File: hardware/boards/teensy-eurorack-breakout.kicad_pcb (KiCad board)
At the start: 2 copper layers, 64.8 x 109.2 mm, 33 parts, among them J1 Conn_01x08, J2 Conn_01x20, J3 Conn_01x20, SW1 Rotary_Encoder_Switch

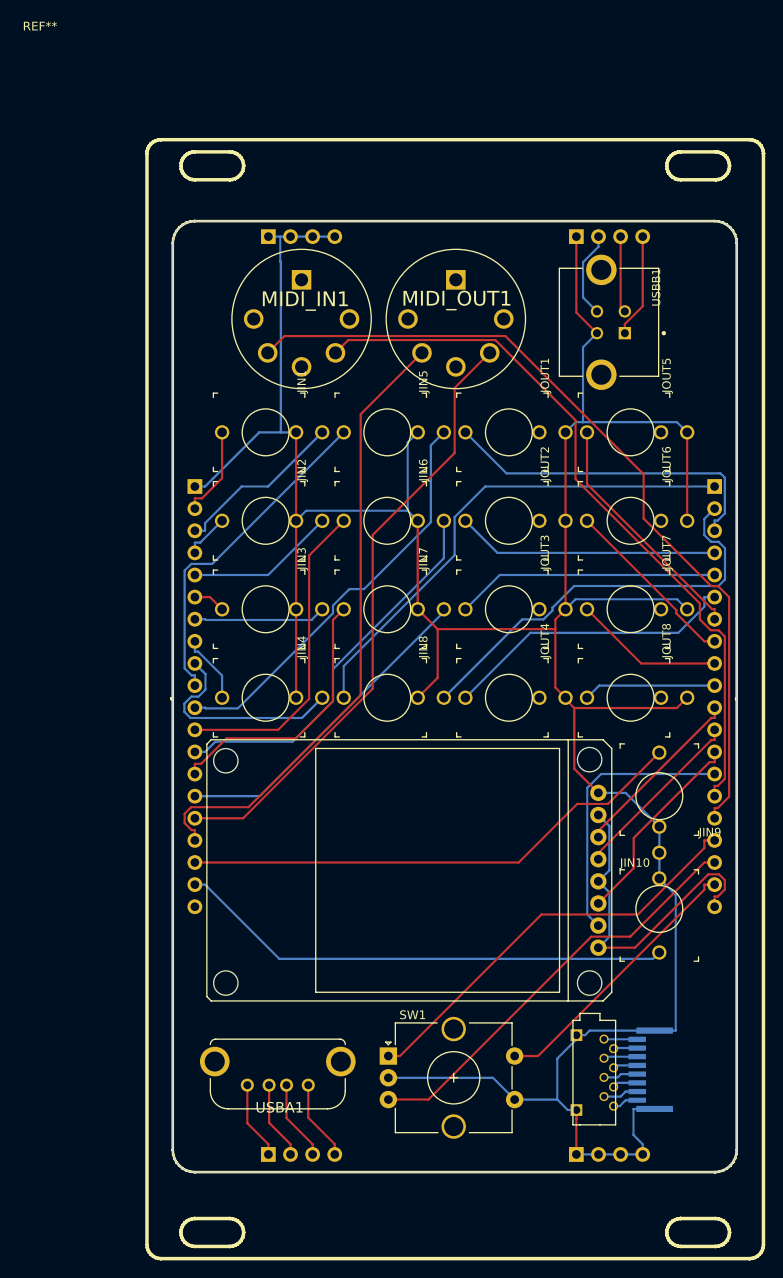
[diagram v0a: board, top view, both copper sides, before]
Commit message: Added jlcpcb parts and changed PCB to 10HP
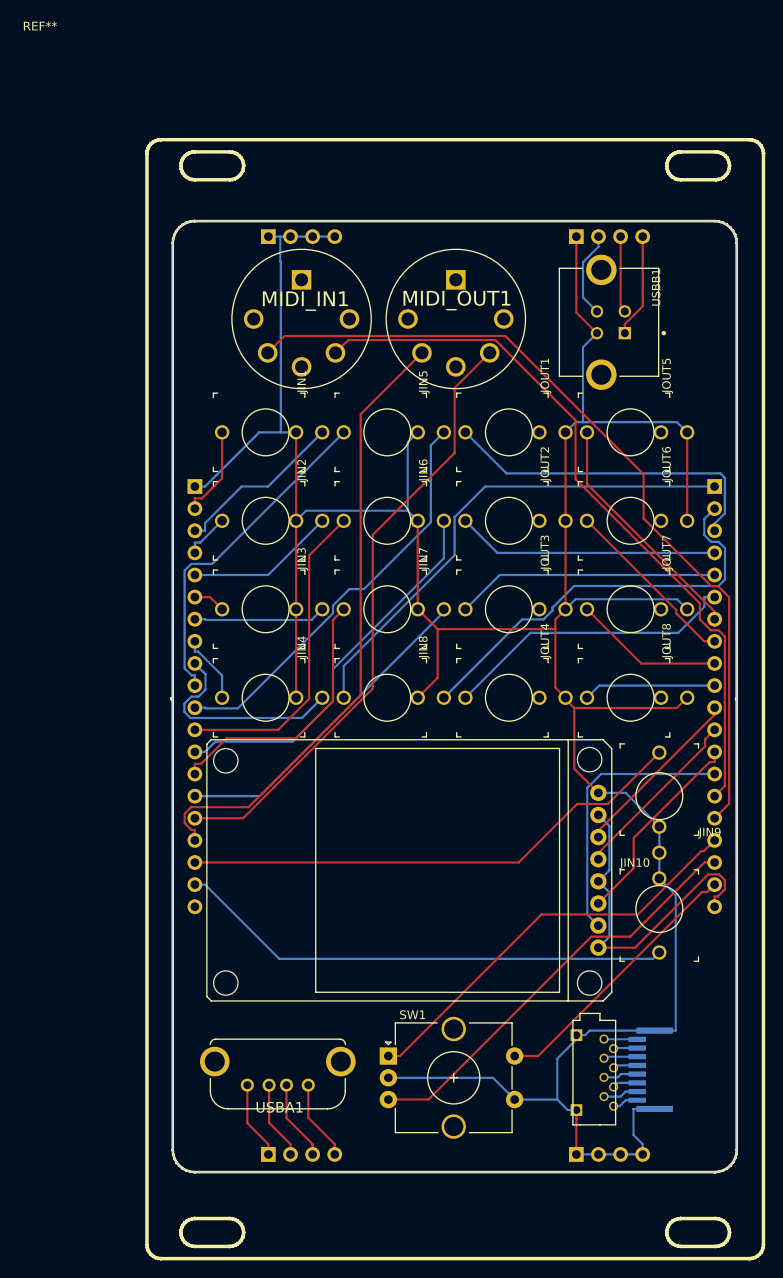
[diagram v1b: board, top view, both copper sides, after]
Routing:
- net /ENC1A: track 48.2 -> 47.7 mm
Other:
- net class Default removed
